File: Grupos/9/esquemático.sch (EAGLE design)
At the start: 28 parts, among them Q1 MMBT4403LT1SMD, Q3 MMBT4403LT1SMD, U3 AP2210N-4.0TRG1, X1 MKDSN1,5/2-5,08, X2 MKDSN1,5/2-5,08, X3 MKDSN1,5/2-5,08, X4 MKDSN1,5/2-5,08

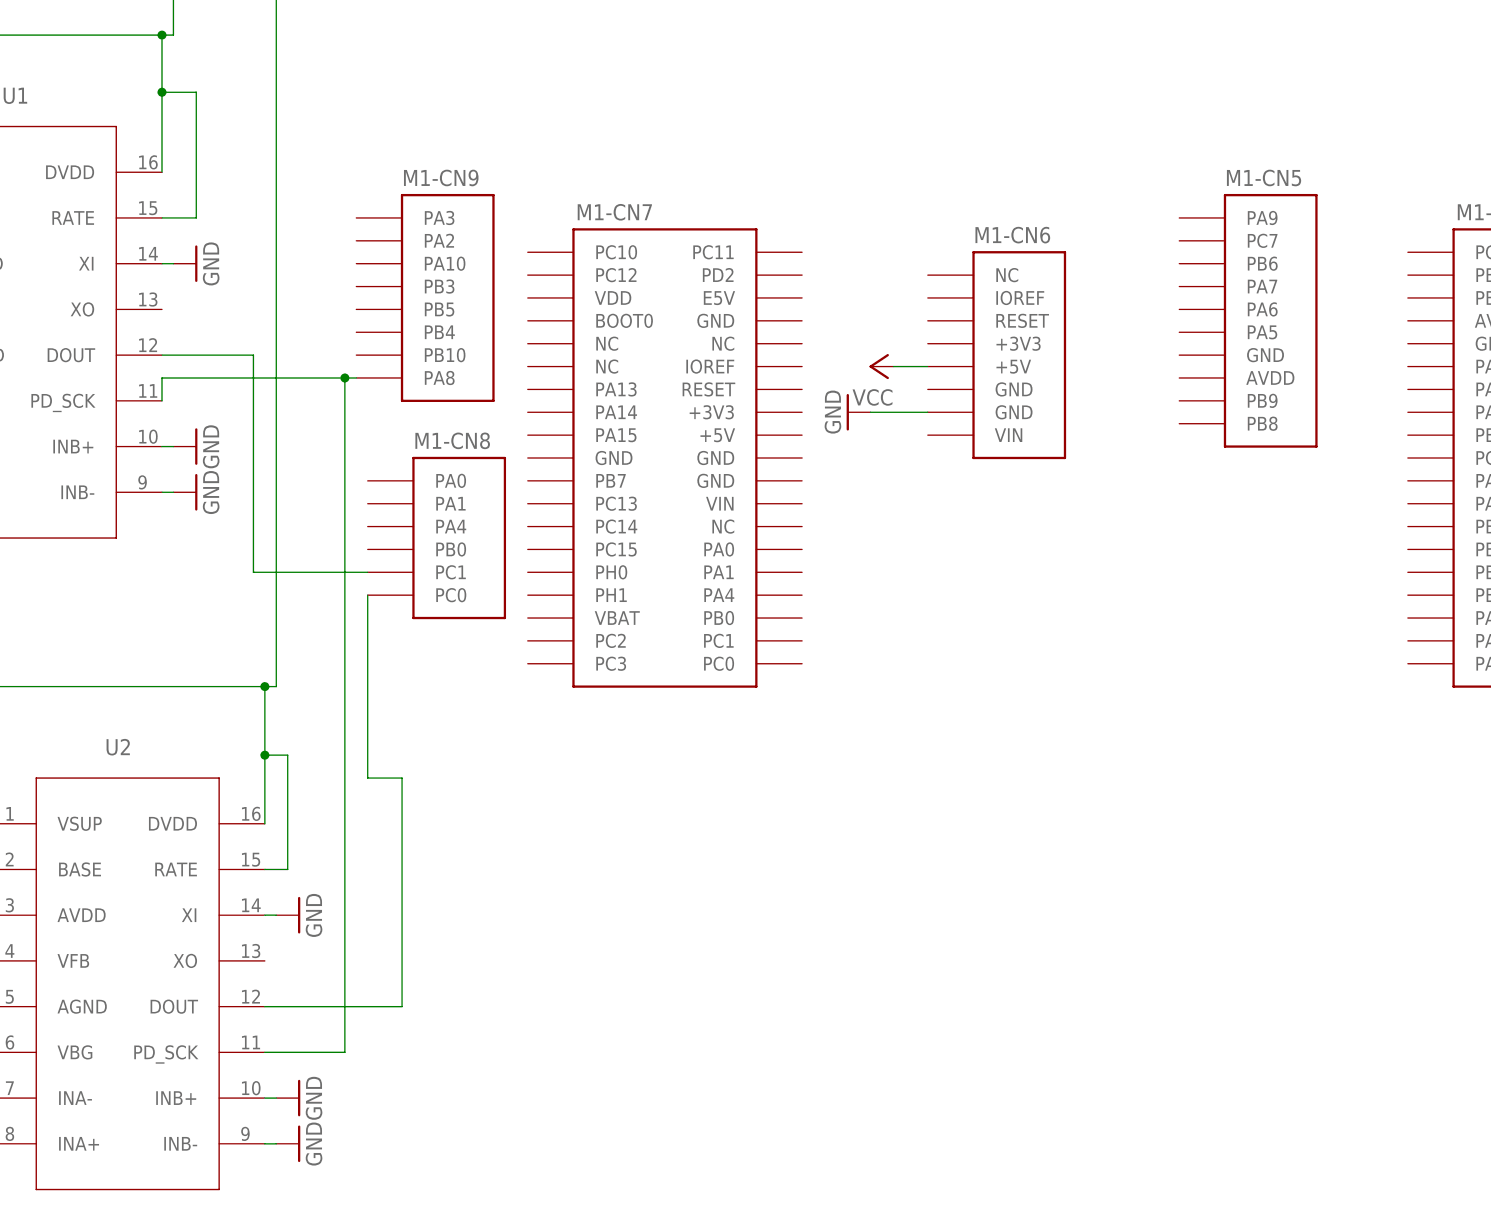
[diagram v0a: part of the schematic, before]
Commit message: Se cablean los ADC a SPI1 y SPI2
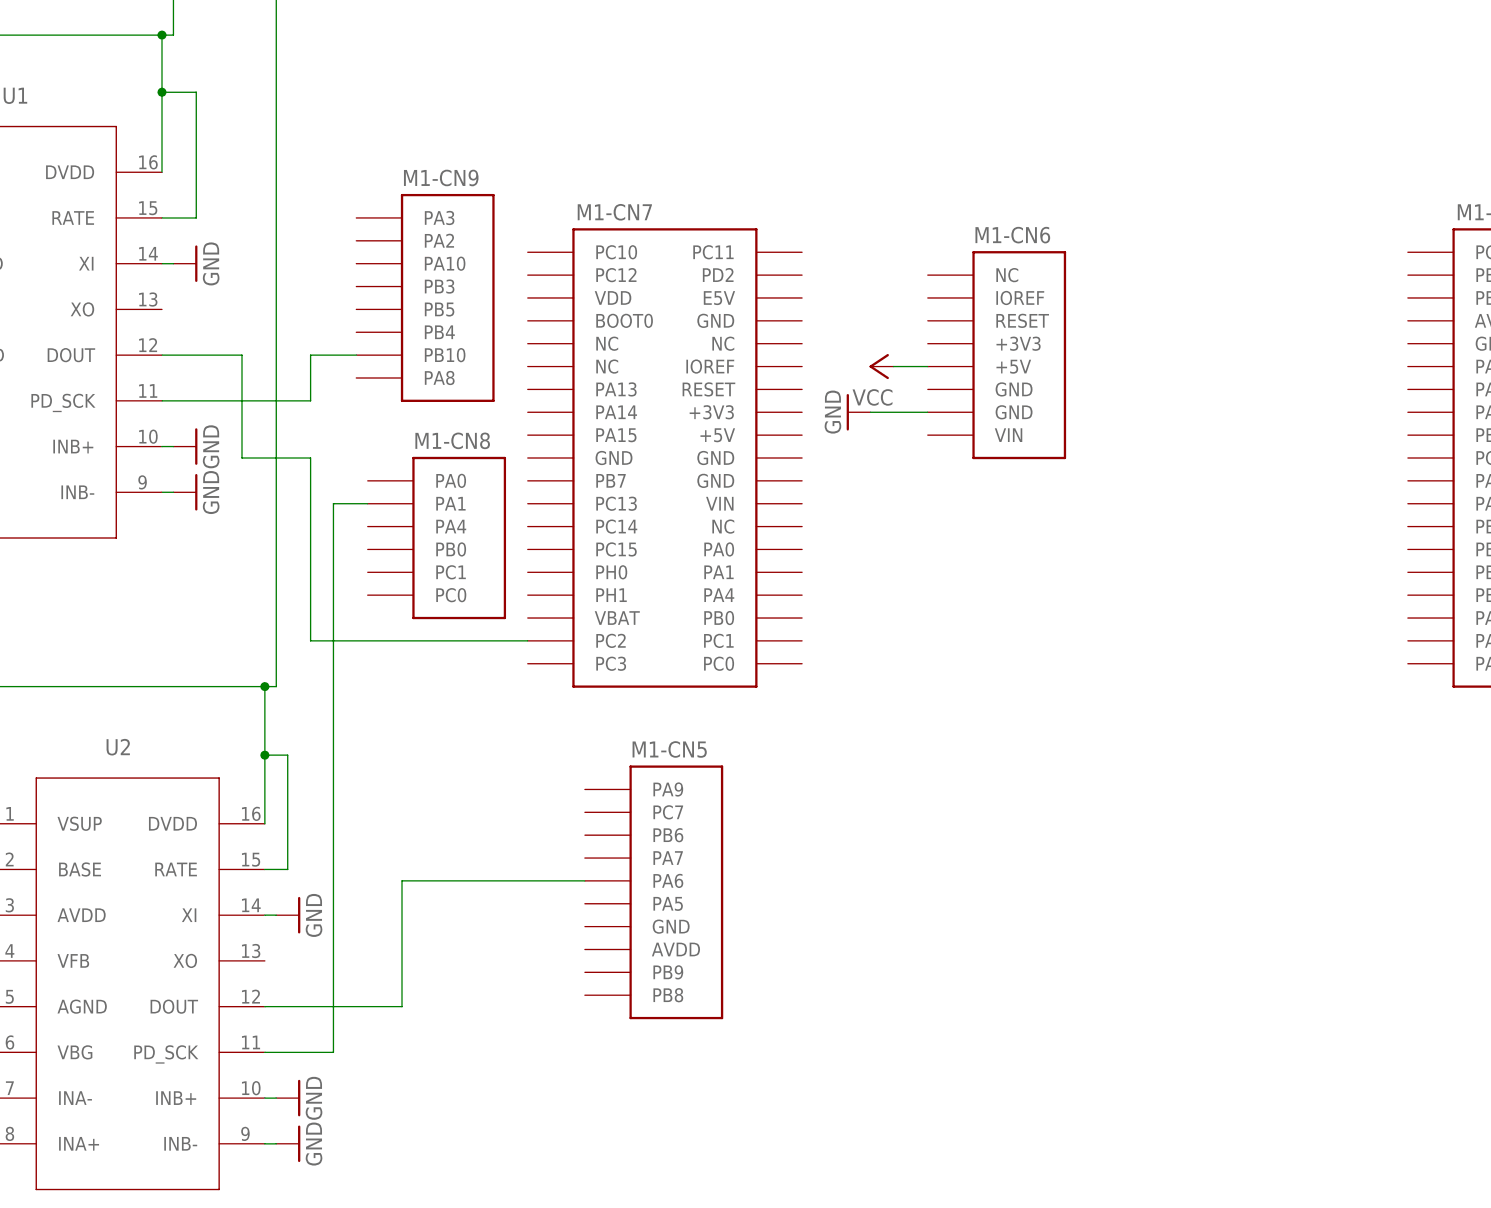
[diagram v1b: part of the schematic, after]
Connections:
- removed net N$20: M1-CN8.PC0, U2.DOUT
- new net N$17: M1-CN5.PA6, U2.DOUT
- new net N$21: M1-CN8.PA1, U2.PD_SCK
- net N$19: now also M1-CN7.PC2; no longer M1-CN8.PC1
- net N$3: now also M1-CN9.PB10; no longer M1-CN9.PA8, U2.PD_SCK
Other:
- moved on the sheet: M1-CN5
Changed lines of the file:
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@@
 <drawing>
 <settings>
-<setting alwaysvectorfont="no"/>
+<setting alwaysvectorfont="yes"/>
 <setting verticaltext="up"/>
 </settings>
-<grid distance="0.05" unitdist="inch" unit="inch" style="lines" multiple="1" display="no" altdistance="0.01" altunitdist="inch" altunit="inch"/>
+<grid distance="0.1" unitdist="inch" unit="inch" style="lines" multiple="1" display="no" altdistance="0.01" altunitdist="inch" altunit="inch"/>
 <layers>
 <layer number="1" name="Top" color="4" fill="1" visible="no" active="no"/>
@@
 <attribute name="NAME" x="104.14" y="65.786" size="1.778" layer="95"/>
 </instance>
-<instance part="M1" gate="-CN5" x="198.12" y="49.53" smashed="yes">
-<attribute name="NAME" x="195.58" y="65.786" size="1.778" layer="95"/>
+<instance part="M1" gate="-CN5" x="132.08" y="-13.97" smashed="yes">
+<attribute name="NAME" x="129.54" y="2.286" size="1.778" layer="95"/>
 </instance>
 <instance part="M1" gate="-CN10" x="231.14" y="35.56" smashed="yes">
@@
 <wire x1="48.26" y1="-10.16" x2="58.42" y2="-10.16" width="0.1524" layer="91"/>
 <pinref part="Q1" gate="G$1" pin="B"/>
-</segment>
-</net>
-<net name="N$3" class="0">
-<segment>
-<pinref part="M1" gate="-CN9" pin="PA8"/>
-<pinref part="U1" gate="ADC$1" pin="PD_SCK"/>
-<wire x1="99.06" y1="44.45" x2="97.79" y2="44.45" width="0.1524" layer="91"/>
-<wire x1="97.79" y1="44.45" x2="77.47" y2="44.45" width="0.1524" layer="91"/>
-<wire x1="77.47" y1="44.45" x2="77.47" y2="41.91" width="0.1524" layer="91"/>
-<pinref part="U2" gate="ADC$1" pin="PD_SCK"/>
-<wire x1="88.9" y1="-30.48" x2="97.79" y2="-30.48" width="0.1524" layer="91"/>
-<wire x1="97.79" y1="-30.48" x2="97.79" y2="44.45" width="0.1524" layer="91"/>
-<junction x="97.79" y="44.45"/>
-</segment>
-</net>
-<net name="N$19" class="0">
-<segment>
-<pinref part="U1" gate="ADC$1" pin="DOUT"/>
-<wire x1="77.47" y1="46.99" x2="87.63" y2="46.99" width="0.1524" layer="91"/>
-<wire x1="87.63" y1="46.99" x2="87.63" y2="22.86" width="0.1524" layer="91"/>
-<pinref part="M1" gate="-CN8" pin="PC1"/>
-<wire x1="87.63" y1="22.86" x2="100.33" y2="22.86" width="0.1524" layer="91"/>
-</segment>
-</net>
-<net name="N$20" class="0">
-<segment>
-<pinref part="M1" gate="-CN8" pin="PC0"/>
-<wire x1="100.33" y1="20.32" x2="100.33" y2="0" width="0.1524" layer="91"/>
-<wire x1="100.33" y1="0" x2="104.14" y2="0" width="0.1524" layer="91"/>
-<wire x1="104.14" y1="0" x2="104.14" y2="-25.4" width="0.1524" layer="91"/>
-<pinref part="U2" gate="ADC$1" pin="DOUT"/>
-<wire x1="104.14" y1="-25.4" x2="88.9" y2="-25.4" width="0.1524" layer="91"/>
 </segment>
 </net>
@@
 </segment>
 </net>
+<net name="N$17" class="0">
+<segment>
+<pinref part="U2" gate="ADC$1" pin="DOUT"/>
+<wire x1="104.14" y1="-25.4" x2="88.9" y2="-25.4" width="0.1524" layer="91"/>
+<pinref part="M1" gate="-CN5" pin="PA6"/>
+<wire x1="104.14" y1="-25.4" x2="104.14" y2="-11.43" width="0.1524" layer="91"/>
+<wire x1="104.14" y1="-11.43" x2="124.46" y2="-11.43" width="0.1524" layer="91"/>
+</segment>
+</net>
+<net name="N$21" class="0">
+<segment>
+<pinref part="U2" gate="ADC$1" pin="PD_SCK"/>
+<wire x1="88.9" y1="-30.48" x2="96.52" y2="-30.48" width="0.1524" layer="91"/>
+<pinref part="M1" gate="-CN8" pin="PA1"/>
+<wire x1="96.52" y1="-30.48" x2="96.52" y2="30.48" width="0.1524" layer="91"/>
+<wire x1="96.52" y1="30.48" x2="100.33" y2="30.48" width="0.1524" layer="91"/>
+</segment>
+</net>
+<net name="N$3" class="0">
+<segment>
+<pinref part="U1" gate="ADC$1" pin="PD_SCK"/>
+<wire x1="77.47" y1="41.91" x2="93.98" y2="41.91" width="0.1524" layer="91"/>
+<wire x1="93.98" y1="41.91" x2="93.98" y2="46.99" width="0.1524" layer="91"/>
+<pinref part="M1" gate="-CN9" pin="PB10"/>
+<wire x1="93.98" y1="46.99" x2="99.06" y2="46.99" width="0.1524" layer="91"/>
+</segment>
+</net>
+<net name="N$19" class="0">
+<segment>
+<pinref part="M1" gate="-CN7" pin="PC2"/>
+<wire x1="118.11" y1="15.24" x2="93.98" y2="15.24" width="0.1524" layer="91"/>
+<wire x1="93.98" y1="15.24" x2="93.98" y2="35.56" width="0.1524" layer="91"/>
+<wire x1="93.98" y1="35.56" x2="86.36" y2="35.56" width="0.1524" layer="91"/>
+<wire x1="86.36" y1="35.56" x2="86.36" y2="46.99" width="0.1524" layer="91"/>
+<pinref part="U1" gate="ADC$1" pin="DOUT"/>
+<wire x1="86.36" y1="46.99" x2="77.47" y2="46.99" width="0.1524" layer="91"/>
+</segment>
+</net>
